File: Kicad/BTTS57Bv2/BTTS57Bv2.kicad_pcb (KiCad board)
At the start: 2 copper layers, 56 x 56 mm, 74 parts, among them P1 Conn_01x06, P2 Conn_01x04, P4 Conn_01x08, P5 Conn_01x02, U2 A4950E, U3 EL-0631, U4 A4950E, U6 EL357NC, U7 STM32F103CBTx, U9 PCA82C251, p7 Conn_01x08

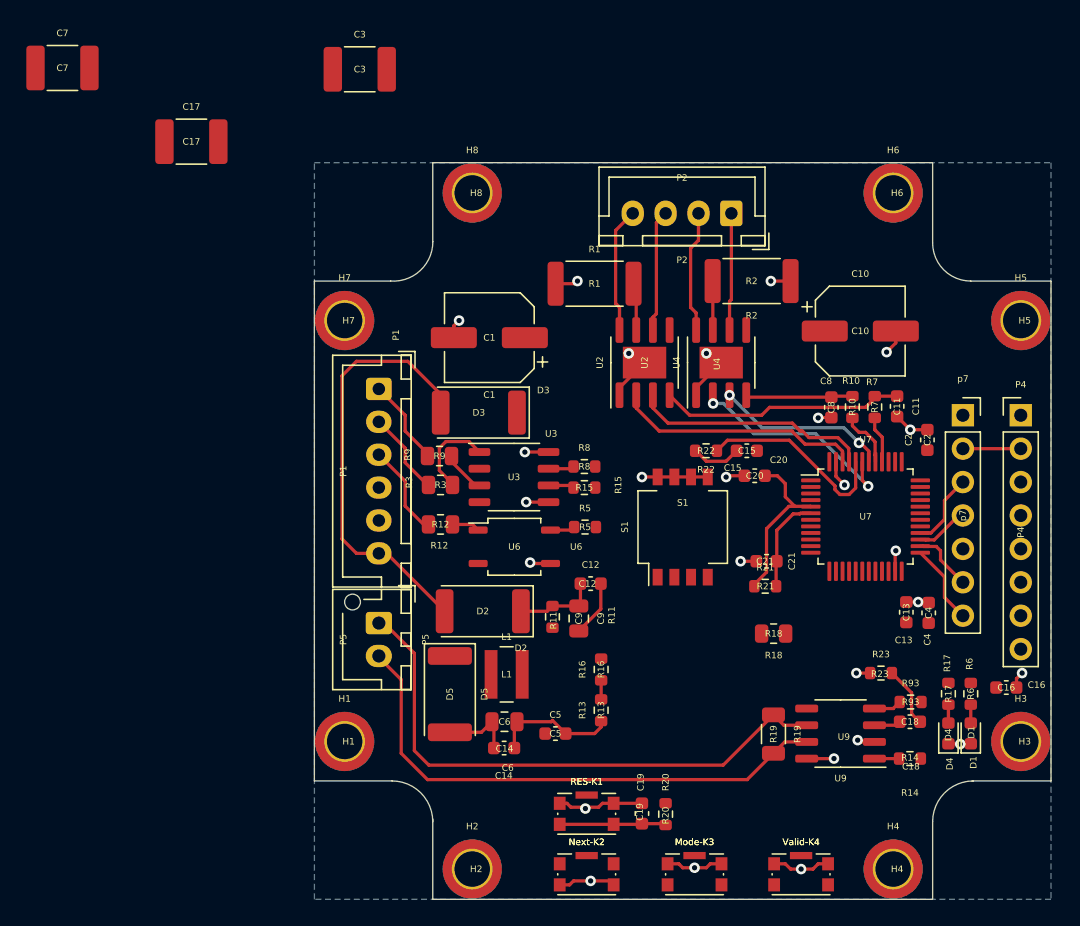
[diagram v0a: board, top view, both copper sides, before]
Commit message: bug fix : wrong pin count order on optical tranceivers
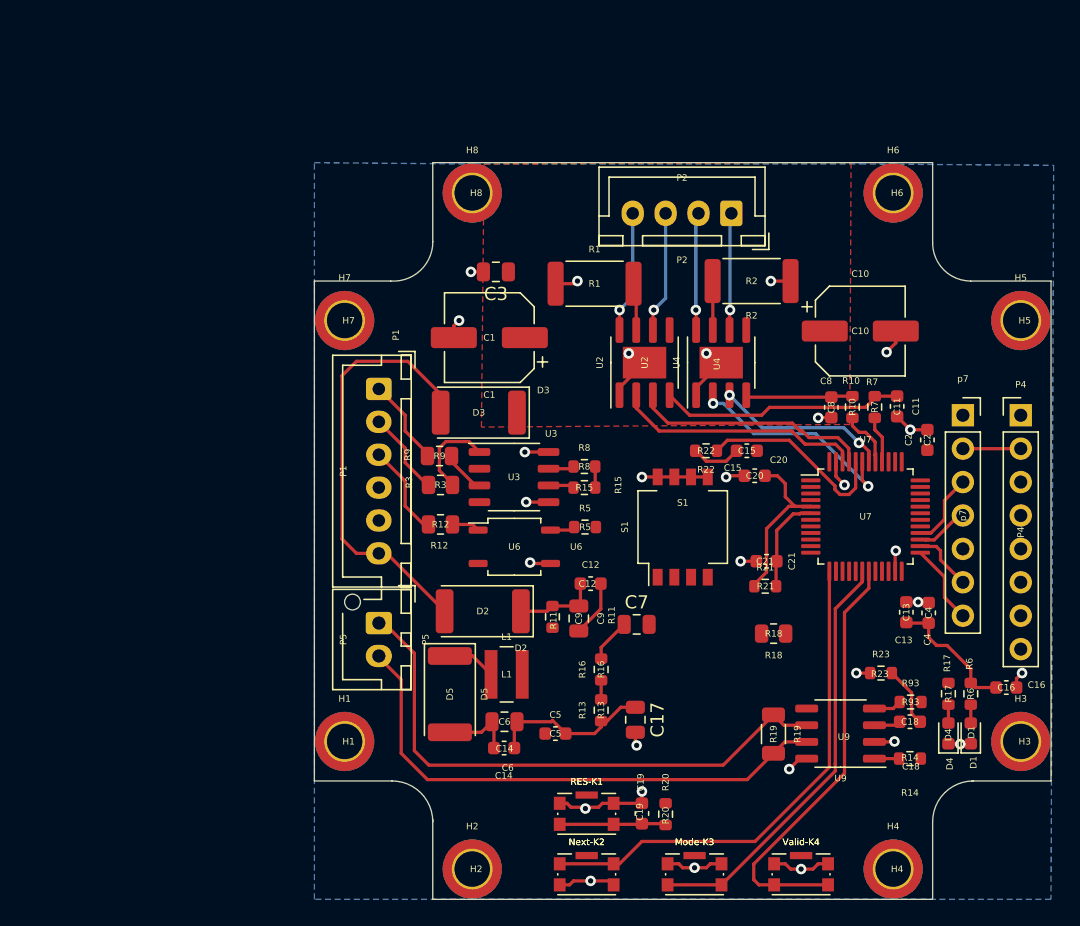
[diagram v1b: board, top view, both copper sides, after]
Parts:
- C17, C3, C7: footprint Capacitor_SMD:C_1812_4532Metric -> Capacitor_SMD:C_0805_2012Metric
- moved C7 60.8 mm to (104.5, 85.1)
- moved C17 55.4 mm to (104.4, 92.3), turned to 270 degrees
- moved C3 18.6 mm to (93.8, 58.3), turned to 180 degrees
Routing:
- net Net-(Next-K2-Pad1): track 0.00 -> 38.4 mm
- net Net-(U7-Pad19): track 0.00 -> 32.9 mm
- net Net-(Mode-K3-Pad2): track 0.00 -> 32.6 mm
- net VDD: track 0.00 -> 11.7 mm
- net Net-(D5-Pad1): track 0.00 -> 3.71 mm
- net Net-(C7-Pad1): track 0.00 -> 3.32 mm
- net +5V: track 9.60 -> 12.6 mm
- net VSS: track 65.2 -> 68.0 mm, vias 26 -> 29
- net Net-(P2-Pad2): track 9.30 -> 8.97 mm, vias 0 -> 1
- net Net-(P2-Pad4): track 9.54 -> 9.29 mm, vias 0 -> 1
- net Net-(P2-Pad3): vias 0 -> 1
- net Net-(P2-Pad1): vias 0 -> 1
- added copper zone on F.Cu, net Net-(C1-Pad1)
